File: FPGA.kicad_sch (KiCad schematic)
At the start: 62 parts, among them IC5 AD817ARZ, IC8 MT25QL128ABA1ESE-0SIT, J13 Conn_02x06_Top_Bottom, J16 Conn_01x02, J17 Conn_02x02_Odd_Even, J3 Conn_01x02, J4 Conn_02x05_Odd_Even, J5 Conn_01x02, J8 Conn_02x06_Top_Bottom, SW1 HARWIN_M50-1900005, SW10 HARWIN_M50-1900005, SW2 HARWIN_M50-1900005, SW8 HARWIN_M50-1900005, SW9 HARWIN_M50-1900005, U4 ICE5LP1K-SG48, U9 LTC2451xDDB

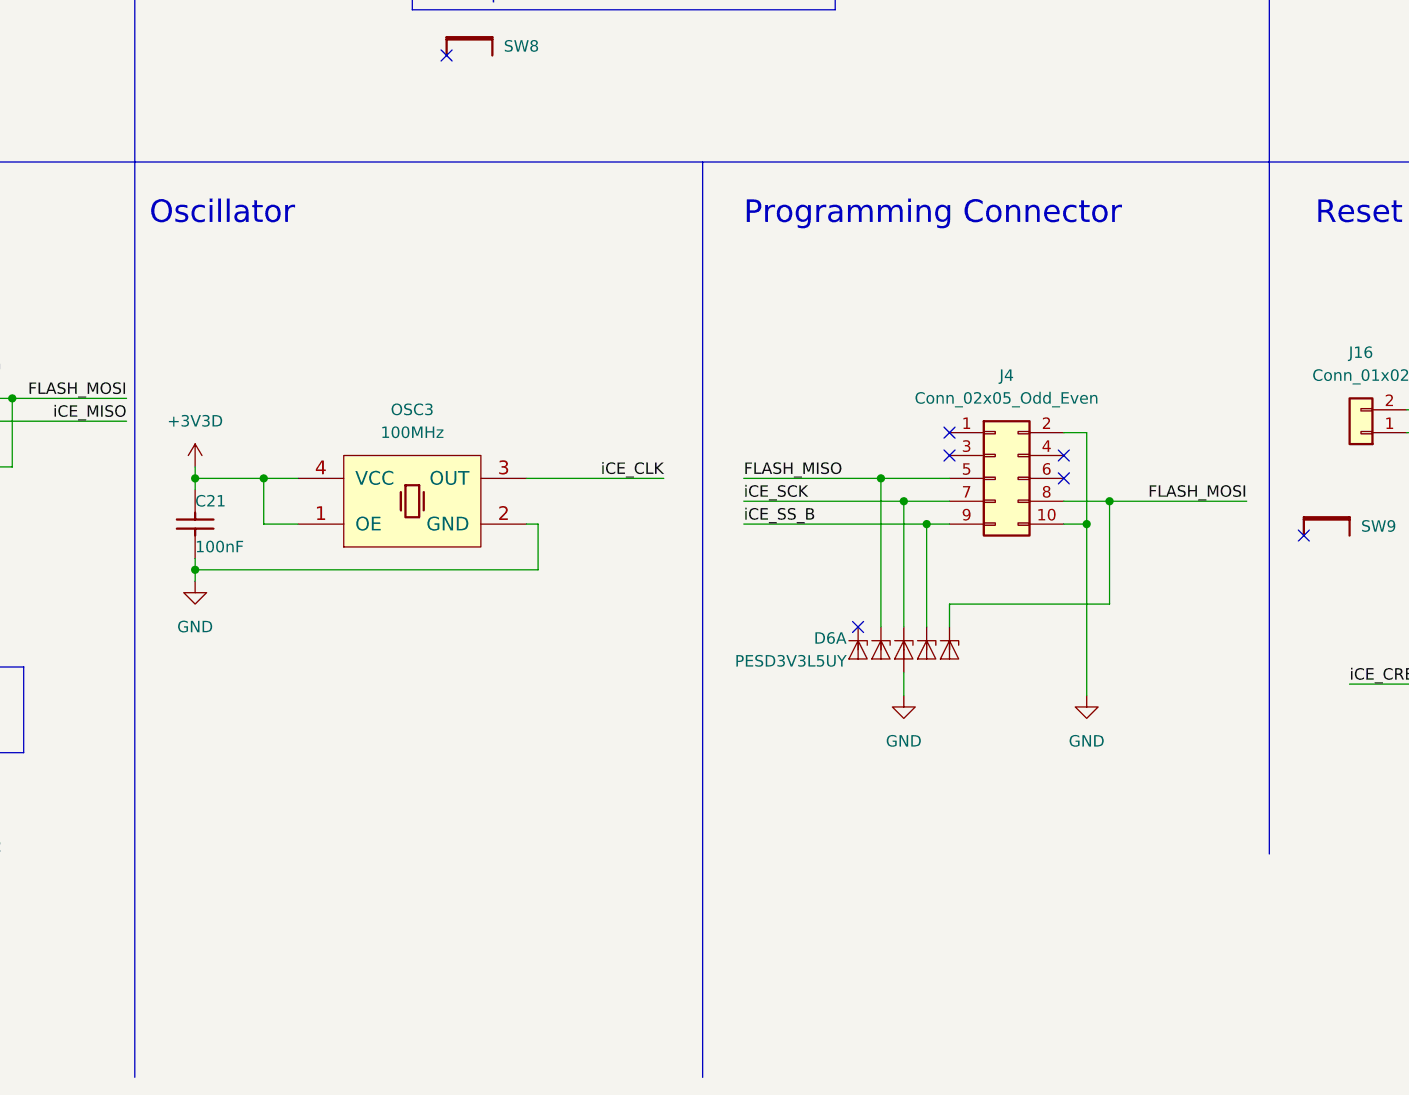
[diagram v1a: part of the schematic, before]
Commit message: Switched RX and TX on FTDI chip, removed FPGA programming connector
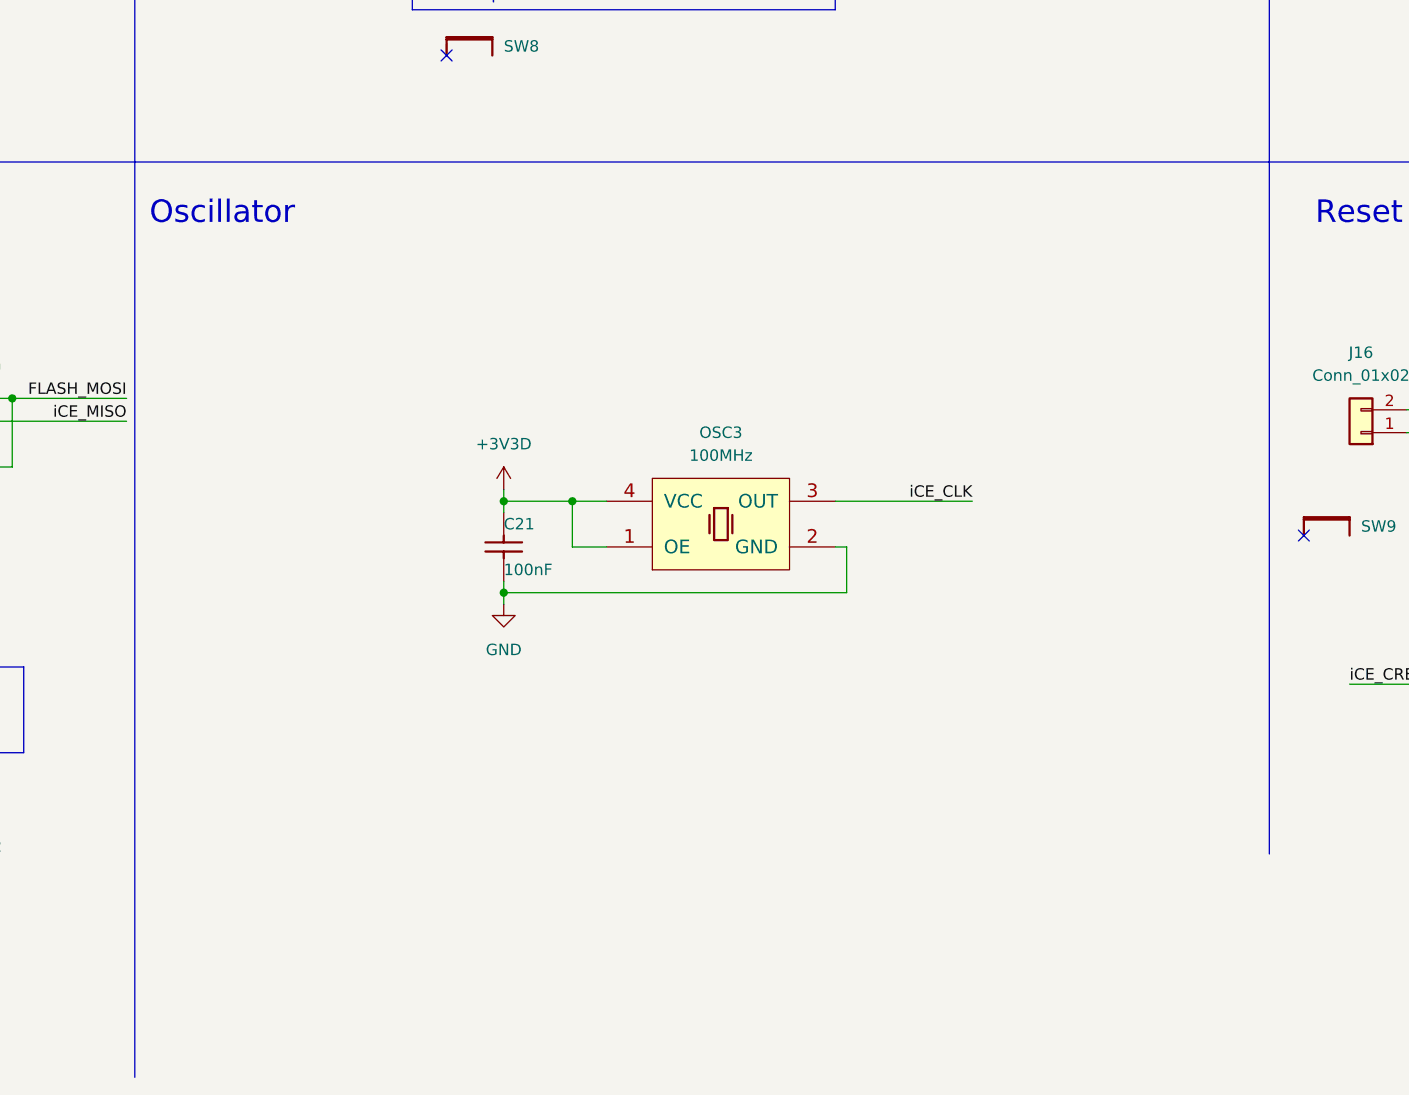
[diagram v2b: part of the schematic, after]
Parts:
- removed D6: PESD3V3L5UY, Package_TO_SOT_SMD:SOT-363_SC-70-6, symbol Power_Protection:PESD3V3L5UY
- removed J4: Conn_02x05_Odd_Even, Connector_PinHeader_2.54mm:PinHeader_2x05_P2.54mm_Vertical, symbol Connector_Generic:Conn_02x05_Odd_Even
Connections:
- no-connect marks 13 -> 8
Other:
- note removed: "Programming Connector"
- moved on the sheet: C21, OSC3

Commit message: Updated template, readded FPGA prog conn
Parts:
- removed C20 (x2), C24: CC0603_10UF_25V_20%_X5R, Capacitors SMD:CAPC1709X100N, symbol Capacitors SMD:CC0603_10UF_25V_20%_X5R
- removed C21 (x3), C25: CC0603_100NF_50V_10%_X7R, Capacitors SMD:CAPC1608X87N, symbol Capacitors SMD:CC0603_100NF_50V_10%_X7R
- removed IC5: AD817ARZ, ICs And Semiconductors SMD:SOIC127P600X175-8N, symbol Operational Amplifiers:AD817ARZ
- removed R50: R0603_1K_0.1%_0.1W_25PPM, Resistors SMD:RESC1608X64N, symbol Resistors SMD:R0603_1K_0.1%_0.1W_25PPM
- removed U9: LTC2451xDDB, Package_DFN_QFN:DFN-8-1EP_2x3mm_P0.5mm_EP0.56x2.15mm, symbol Analog_ADC:LTC2451xDDB
- added D6: PESD3V3L5UY, Package_TO_SOT_SMD:SOT-363_SC-70-6, symbol Power_Protection:PESD3V3L5UY
- added J1: Conn_02x05_Odd_Even, Connector_PinHeader_2.54mm:PinHeader_2x05_P2.54mm_Vertical, symbol Connector_Generic:Conn_02x05_Odd_Even
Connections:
- net ADBUS0: now also D6.1 (K1), J1.7 (Pin_7)
- net ADBUS1: now also D6.4 (K3), J1.8 (Pin_8)
- net ADBUS2: now also D6.6 (K5), J1.5 (Pin_5)
- net ADBUS4: now also D6.3 (K2), J1.9 (Pin_9)
- net GND: now also D6.2 (A), J1.10 (Pin_10), J1.2 (Pin_2)
- no-connect marks 8 -> 11
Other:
- note added: "Programming Connector"
- note removed: "OTA ADC"
- moved on the sheet: C21, D1, D13, J13, J16, J5, J8, LD1, OSC3, PB1, R15, R16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

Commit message: Split I2C buses, FPGA2MCU has its own now
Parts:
- removed D1: SMBJ3V3, ICs And Semiconductors SMD:DIOM5436X244N, symbol Diodes:SMBJ3V3
- removed J13: Conn_02x06_Top_Bottom, Connector_PinSocket_2.54mm:PinSocket_2x06_P2.54mm_Vertical, symbol Connector_Generic:Conn_02x06_Top_Bottom
- removed J16: Conn_01x02, Connector_PinHeader_2.54mm:PinHeader_1x02_P2.54mm_Vertical, symbol Connector_Generic:Conn_01x02
- removed PB1: PB_C&K_KSC321JLFS, Switches:PB_C&K_KSC321J, symbol Switches:PB_C&K_KSC321JLFS
- removed R26: R0603_2K2_1%_0.1W_100PPM, Resistors SMD:RESC1608X55N, symbol Resistors SMD:R0603_2K2_1%_0.1W_100PPM
- removed R52: R0603_10K_1%_0.1W_100PPM, Resistors SMD:RESC1608X55N, symbol Resistors SMD:R0603_10K_1%_0.1W_100PPM
- removed SW9: HARWIN_M50-1900005, symbol HARWIN:HARWIN_M50-1900005
- added J4: Conn_01x06, symbol Connector_Generic:Conn_01x06
- added R32: R0603_1K0_0.1%_0.063W_10PPM, Resistors SMD:RESC1608X55N, symbol Resistors SMD:R0603_1K0_0.1%_0.063W_10PPM
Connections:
- net ADBUS7 is gone; now on net RESET: U4.8 (~{CRESET})
- net +3V3D: now also J4.6 (Pin_6), R32.1
- net GND: now also J4.5 (Pin_5)
- net IOB_22: now also J4.1 (Pin_1)
- net IOB_23: now also J4.2 (Pin_2)
- net IOB_24: now also J4.3 (Pin_3)
- net IOB_25: now also J4.4 (Pin_4)
- net RESET: no longer U4.34 (IOT_44b)
- net at J5.2 (Pin_2), LD1.2 (A): now also R32.2
- net IOB_13 renamed F2M_PA12
- net IOB_16 renamed F2M_PA13
- net IOB_18: no longer names the net of U4.10 (IOB_18a)
- net IOB_20: no longer names the net of U4.11 (IOB_20a)
- new net ACCURATE_RESET: U4.34 (IOT_44b)
- no-connect marks 11 -> 12
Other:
- note removed: "Reset"
- moved on the sheet: C21, D1, D13, D6A, IC8, J1, J3, J8, R15, R16, R22, R23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

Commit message: Fixed some DRC errors and warings
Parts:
- removed J4: Conn_01x06, symbol Connector_Generic:Conn_01x06
- added D7: 1N4148WS, Diode_THT:D_DO-41_SOD81_P7.62mm_Horizontal, symbol Diodes:1N4148WS
- added J4: Conn_02x06_Top_Bottom, Connector_PinSocket_2.54mm:PinSocket_2x06_P2.54mm_Vertical, symbol Connector_Generic:Conn_02x06_Top_Bottom
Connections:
- net FPGA_RxD is gone; now on net FPGA_RX: U4.42 (IOT_51a)
- net FPGA_TxD is gone; now on net FPGA_TX: U4.38 (IOT_50b)
- net MCU_SCL is gone; now on net F2M_PA13: U4.18 (IOB_31b)
- net MCU_SDA is gone; now on net F2M_PA12: U4.19 (IOB_29b)
- net +3V3D: now also J4.12 (Pin_12), J4.6 (Pin_6)
- net F2M_PA12: no longer U4.6 (IOB_13b)
- net F2M_PA13: no longer U4.9 (IOB_16a)
- net GND: now also J4.11 (Pin_11), J4.5 (Pin_5)
- net IOB_22: now also J4.7 (Pin_7)
- net IOB_23: now also J4.8 (Pin_8)
- net IOB_24: now also J4.9 (Pin_9)
- net IOB_25: now also J4.10 (Pin_10)
- net RESET: now also D7.2 (A); no longer U4.8 (~{CRESET})
- net IOB_18: now reaches U4.10 (IOB_18a)
- net IOB_18: now also J4.3 (Pin_3)
- net IOB_20: now reaches U4.11 (IOB_20a)
- net IOB_20: now also J4.4 (Pin_4)
- new net ADBUS7: D7.1 (C), U4.8 (~{CRESET})
- new net IOB_13: J4.1 (Pin_1), U4.6 (IOB_13b)
- new net IOB_16: J4.2 (Pin_2), U4.9 (IOB_16a)
- no-connect marks 12 -> 10
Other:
- moved on the sheet: C21

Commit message: Reannotated schematic, added PSU calculation, some polish
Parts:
- renumbered C21 to C?, C20 to C?, C2 to C?, D13 to D10, D6 to D?, D1 to D?, D7 to D?, IC8 to IC10, U4 to IC9, J17 to J10, J3 to J11, J1 to J12, J5 to J13, J8 to J14, J4 to J15, LD1 to LD12, OSC3 to OSC2, R24 to R33, R23 to R34, R25 to R35, R22 to R36, R51 to R38, R15 to R39, R16 to R40, R40 to R41, R44 to R?, R45 to R?, R32 to R?, SW1 to SW4, SW2 to SW5, SW8 to SW6, SW10 to SW7, TP4 to TP?
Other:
- moved on the sheet: C?, OSC2

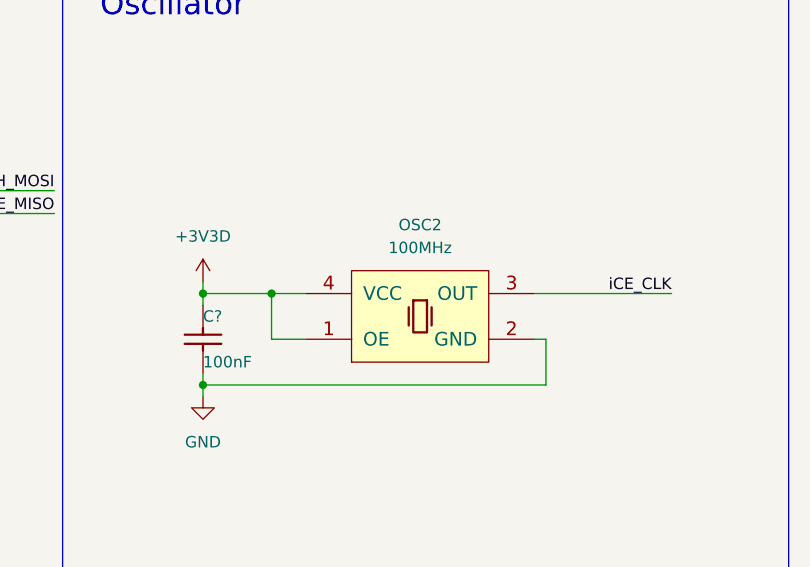
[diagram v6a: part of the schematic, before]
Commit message: Replaced TP1 and FPGA oscillator
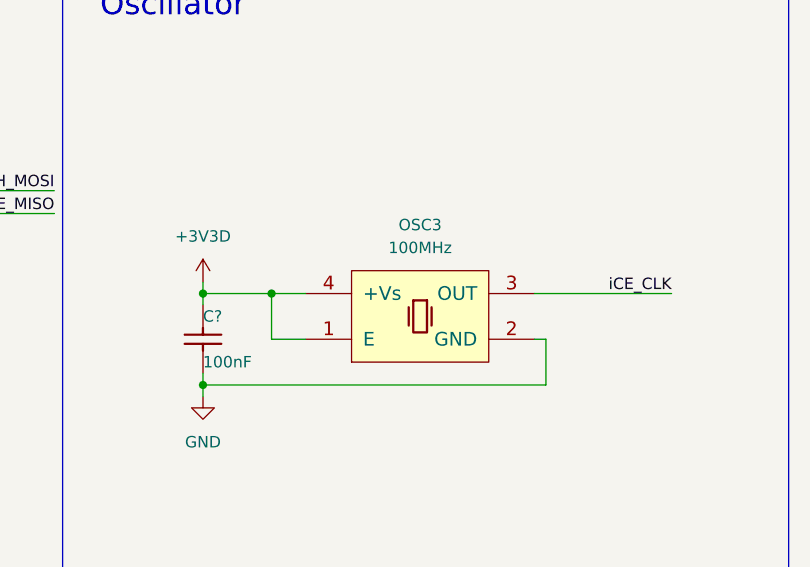
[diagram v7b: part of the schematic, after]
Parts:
- removed OSC2: OSC_100MHZ_EPSON_SG-8002CAPCB100MHZ, ICs And Semiconductors SMD:OSC_EPSON_SG-8002CA, symbol Crystals & Oscillators:OSC_100MHZ_EPSON_SG-8002CAPCB100MHZ
- added OSC3: OSC_100MHZ_IQD_LFSPXO022731, ICs And Semiconductors SMD:OSC_IQD_CFPS-73, symbol Crystals & Oscillators:OSC_100MHZ_IQD_LFSPXO022731
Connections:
- net +3V3D: now also OSC3.1 (E), OSC3.4 (+Vs)
- net GND: now also OSC3.2 (GND)
- net iCE_CLK: now also OSC3.3 (OUT)

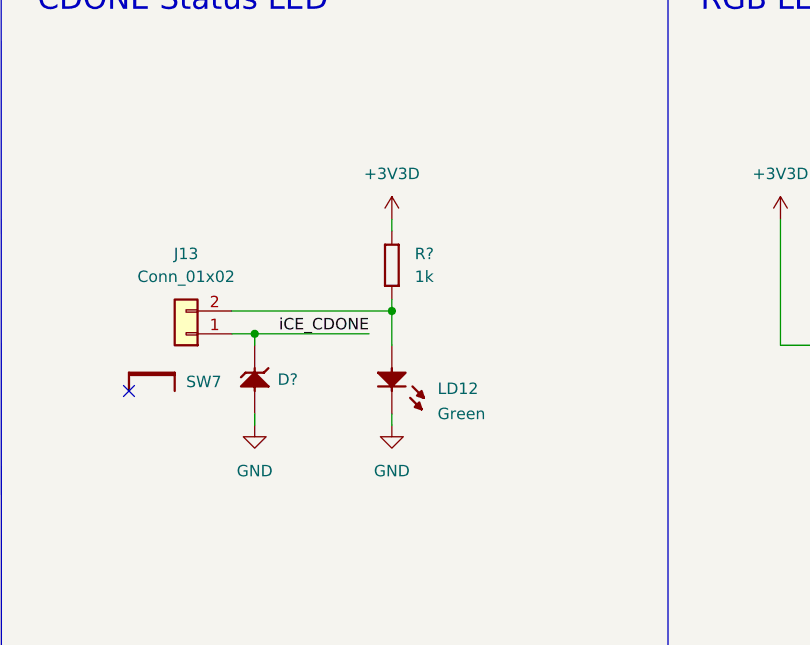
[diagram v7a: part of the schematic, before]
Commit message: Added USB connector, EEPROM, and replaced 2V5 diode
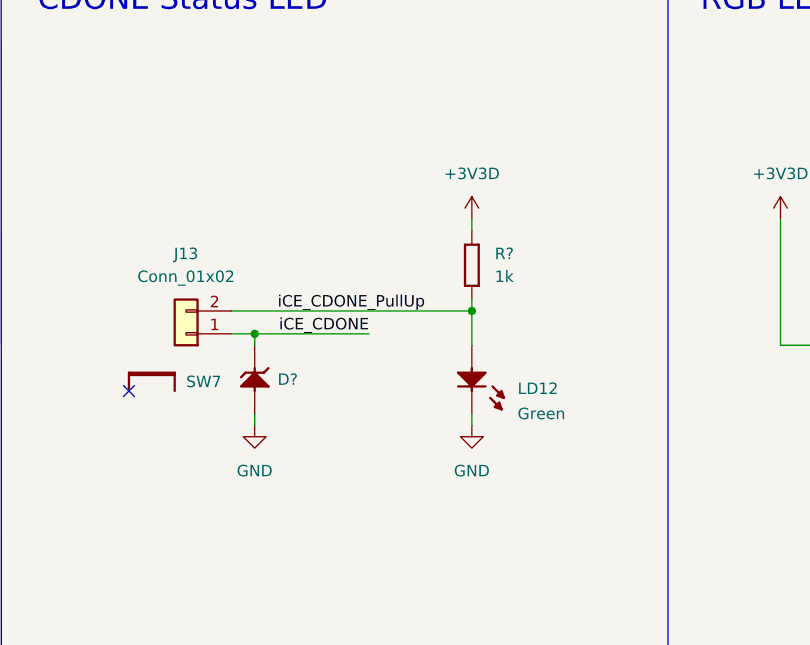
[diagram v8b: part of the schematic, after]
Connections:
- net iCE_CDONE_PullUp: now reaches J13.2 (Pin_2), LD12.2 (A), R?.2
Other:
- moved on the sheet: LD12, R?
